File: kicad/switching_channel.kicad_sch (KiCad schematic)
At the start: 6 parts, among them U1 SN74LVC1G17DCKR, U6 UCC23313DWYR, U7 SISS94DN-T1-GE3

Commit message: kicad
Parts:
- renumbered U1 to U23
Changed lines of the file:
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@@
 		(dnp no)
 		(fields_autoplaced yes)
-		(property "Reference" "U1"
+		(property "Reference" "U23"
 			(at 103.505 90.17 0)
 			(effects
@@
 		(instances
 			(project "bidirectional_load_switch"
+				(path "/a4768a02-c961-4971-939f-bbf2bfa51fa3/06372500-caf3-4250-bfb9-ddec4018ea78"
+					(reference "U?")
+					(unit 1)
+				)
 				(path "/a4768a02-c961-4971-939f-bbf2bfa51fa3/2c84e58d-6144-4329-9588-9692af6c916f"
 					(reference "U23")
@@
 		(dnp no)
 		(fields_autoplaced yes)
-		(property "Reference" "#PWR012"
+		(property "Reference" "#PWR036"
 			(at 175.26 116.84 0)
 			(effects
@@
 		(instances
 			(project "bidirectional_load_switch"
+				(path "/a4768a02-c961-4971-939f-bbf2bfa51fa3/06372500-caf3-4250-bfb9-ddec4018ea78"
+					(reference "#PWR?")
+					(unit 1)
+				)
 				(path "/a4768a02-c961-4971-939f-bbf2bfa51fa3/2c84e58d-6144-4329-9588-9692af6c916f"
 					(reference "#PWR036")
@@
 		(dnp no)
 		(fields_autoplaced yes)
-		(property "Reference" "#PWR02"
+		(property "Reference" "#PWR034"
 			(at 118.11 118.11 0)
 			(effects
@@
 		(instances
 			(project "bidirectional_load_switch"
+				(path "/a4768a02-c961-4971-939f-bbf2bfa51fa3/06372500-caf3-4250-bfb9-ddec4018ea78"
+					(reference "#PWR?")
+					(unit 1)
+				)
 				(path "/a4768a02-c961-4971-939f-bbf2bfa51fa3/2c84e58d-6144-4329-9588-9692af6c916f"
 					(reference "#PWR034")

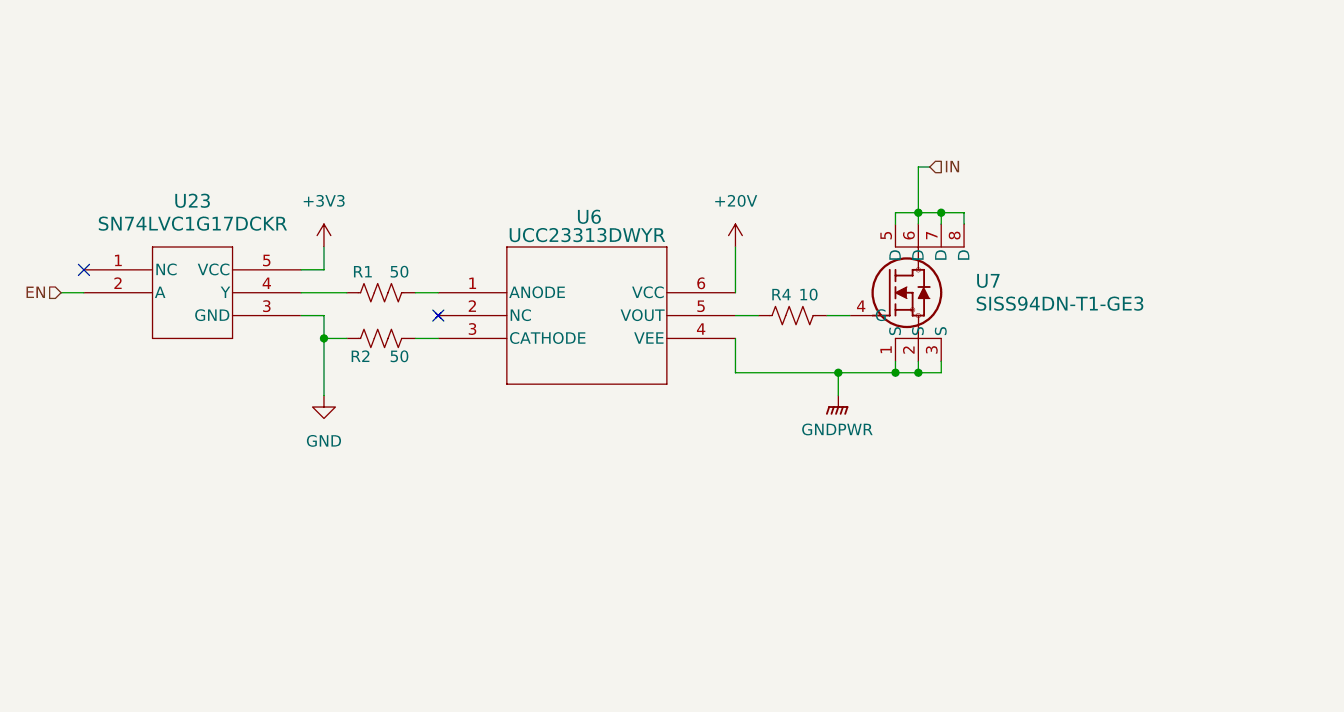
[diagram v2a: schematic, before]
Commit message: updated switch topology
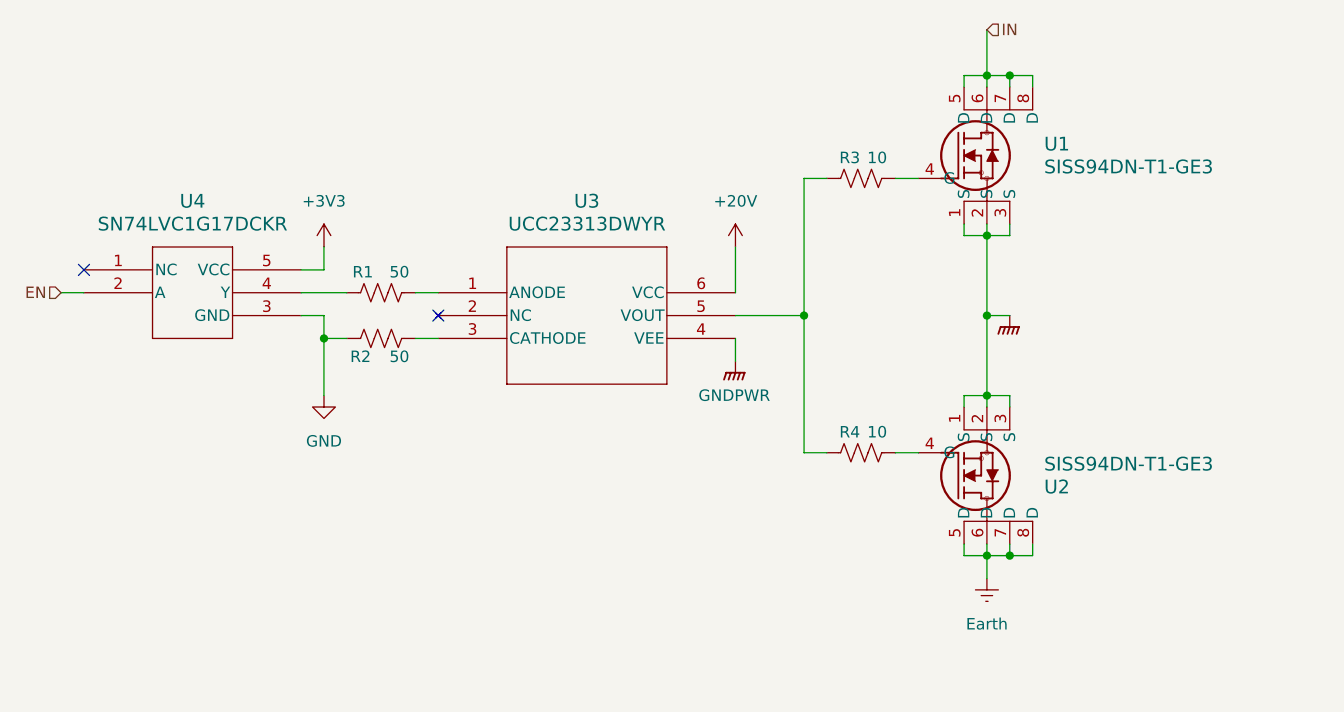
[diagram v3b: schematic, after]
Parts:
- added R3: 10, Resistor_SMD:R_0603_1608Metric_Pad0.98x0.95mm_HandSolder, symbol Device:R_US
- added U2: SISS94DN-T1-GE3, Switching Mosfet:MOSFET_3DN-T1-GE3_VIS, symbol Mosfet:SISS94DN-T1-GE3
- renumbered U7 to U1, U6 to U3, U23 to U4
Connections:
- net GNDPWR: now also U2.1 (S), U2.2 (S), U2.3 (S)
- net at R4.1, U3.5 (VOUT): now also R3.1
- net at U1.4 (G): now also R3.2; no longer R4.2
- new net: R4.2, U2.4 (G)
- new net Earth: U2.5 (D), U2.6 (D), U2.7 (D), U2.8 (D)
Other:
- moved on the sheet: U1

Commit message: kicad
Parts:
- removed U1, U2: SISS94DN-T1-GE3, Switching Mosfet:MOSFET_3DN-T1-GE3_VIS, symbol Mosfet:SISS94DN-T1-GE3
- removed U3: UCC23313DWYR, Gate Driver:SOIC6_DWY_TEX, symbol Gate Driver:UCC23313DWYR
- removed U4: SN74LVC1G17DCKR, Buffer:DCK5, symbol Buffer:SN74LVC1G17DCKR
- added U1: SN74LVC1G17DCKR, DCK5, symbol Buffer:SN74LVC1G17DCKR
- added U2: UCC23313DWYR, SOIC6_DWY_TEX, symbol Gate Driver:UCC23313DWYR
- added U3, U4: SISS94DN-T1-GE3, MOSFET_3DN-T1-GE3_VIS, symbol Switching Mosfet:SISS94DN-T1-GE3
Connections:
- net +3V3: now also U1.5 (VCC)
- net EN: now also U1.2 (A)
- net Earth: now also U4.5 (D), U4.6 (D), U4.7 (D), U4.8 (D)
- net GND: now also U1.3 (GND)
- net GNDPWR: now also U2.4 (VEE), U3.1 (S), U3.2 (S), U3.3 (S), U4.1 (S), U4.2 (S), U4.3 (S)
- net IN: now also U3.5 (D), U3.6 (D), U3.7 (D), U3.8 (D)
- net at R3.1, R4.1: now also U2.5 (VOUT)
- net at R3.2: now also U3.4 (G)
- net at R1.2: now also U2.1 (ANODE)
- net at R2.2: now also U2.3 (CATHODE)
- net at R4.2: now also U4.4 (G)
- net at R1.1: now also U1.4 (Y)
- new net 20V_isolated: U2.6 (VCC)
- no-connect marks 2 -> 0
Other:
- moved on the sheet: R1, R2

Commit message: kicad
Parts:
- added CB1: 1u, symbol Device:C_Small
- added CB2, CB4: 100n, symbol Device:C_Small
- added CB3: 10u, symbol Device:C_Small
- R3, R4: value 10 -> 5
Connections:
- net 20V_isolated: now also CB3.1, CB4.1
- net GND: now also CB1.2, CB2.2
- net GNDPWR: now also CB3.2, CB4.2
- net +3V3 renamed 3v3
- net 3v3: now also CB1.1, CB2.1
- net EN renamed PWM
- net IN renamed RIN
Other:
- moved on the sheet: R3, R4, U3, U4

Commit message: kicad
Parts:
- renumbered U4 to U10, U1 to U6, U2 to U8
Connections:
- net 20V_isolated renamed 15V_isolated

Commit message: kicad
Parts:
- C201: renamed from CB1; footprint (none) -> Capacitor_SMD:C_0402_1005Metric
- C202: renamed from CB2; footprint (none) -> Capacitor_SMD:C_0402_1005Metric
- C203: renamed from CB3; footprint (none) -> Capacitor_SMD:C_1206_3216Metric
- C204: renamed from CB4; footprint (none) -> Capacitor_SMD:C_0402_1005Metric
- U201: renamed from U6; footprint DCK5 -> buffer_SN74LVC1G17DCKR:DCK5
- U202: renamed from U8; footprint SOIC6_DWY_TEX -> gate_driver_UCC23313DWYR:SOIC6_DWY_TEX
- U203: renamed from U3; footprint MOSFET_3DN-T1-GE3_VIS -> mosfet_SISS94DN-T1-GE3:MOSFET_3DN-T1-GE3_VIS
- U204: renamed from U10; footprint MOSFET_3DN-T1-GE3_VIS -> mosfet_SISS94DN-T1-GE3:MOSFET_3DN-T1-GE3_VIS
- renumbered R1 to R201, R2 to R202, R3 to R203, R4 to R204

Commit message: kicad
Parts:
- removed U201: SN74LVC1G17DCKR, buffer_SN74LVC1G17DCKR:DCK5, symbol Buffer:SN74LVC1G17DCKR
- removed U202: UCC23313DWYR, gate_driver_UCC23313DWYR:SOIC6_DWY_TEX, symbol Gate Driver:UCC23313DWYR
- removed U203, U204: SISS94DN-T1-GE3, mosfet_SISS94DN-T1-GE3:MOSFET_3DN-T1-GE3_VIS, symbol Switching Mosfet:SISS94DN-T1-GE3
- added U201: SN74LVC1G17DCKR, DCK5, symbol buffer_SN74LVC1G17DCKR:SN74LVC1G17DCKR
- added U202: UCC23313DWYR, SOIC6_DWY_TEX, symbol gate_driver_UCC23313DWYR:UCC23313DWYR
- added U203, U204: SISS94DN-T1-GE3, MOSFET_3DN-T1-GE3_VIS, symbol mosfet_SISS94DN-T1-GE3:SISS94DN-T1-GE3
- C201: footprint Capacitor_SMD:C_0402_1005Metric -> Capacitor_SMD:C_0603_1608Metric
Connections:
- net 15V_isolated: now also U202.6 (VCC)
- net 3v3: now also U201.5 (VCC)
- net Earth: now also U204.5 (D)
- net GND: now also U201.3 (GND)
- net GNDPWR: now also U202.4 (VEE), U203.1 (S), U203.2 (S), U203.3 (S), U204.1 (S), U204.2 (S), U204.3 (S)
- net PWM: now also U201.2 (A)
- net RIN: now also U203.5 (D)
- net at R204.2: now also U204.4 (G)
- net at R203.1, R204.1: now also U202.5 (VOUT)
- net at R203.2: now also U203.4 (G)
- net at R201.2: now also U202.1 (ANODE)
- net at R202.2: now also U202.3 (CATHODE)
- net at R201.1: now also U201.4 (Y)
